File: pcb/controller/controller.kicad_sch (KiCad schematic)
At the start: 27 parts, among them J1 Conn_01x02, J10 USB_C_Receptacle_USB2.0_16P, J2 Conn_01x02, J3 Conn_01x02, J4 Conn_01x02, J5 Conn_01x02, J6 Conn_01x02, J7 Conn_01x02, J8 RJ45, U2 AP2112K-3.3

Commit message: Final Version of new Controller Rev. 00 (Prototype)
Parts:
- removed C3, C4: C, Capacitor_SMD:C_0805_2012Metric_Pad1.18x1.45mm_HandSolder, symbol Device:C
- removed J1, J2, J3, J4, J5, J6, J7: Conn_01x02, Connector_JST:JST_XH_B2B-XH-AM_1x02_P2.50mm_Vertical, symbol Connector_Generic:Conn_01x02
- removed J10: USB_C_Receptacle_USB2.0_16P, Connector_USB:USB_C_Receptacle_GCT_USB4105-xx-A_16P_TopMnt_Horizontal, symbol Connector:USB_C_Receptacle_USB2.0_16P
- removed J8: RJ45, RJ45:RJ45_Amphenol_54602-x08_Horizontal, symbol Connector:RJ45
- removed JP1: SolderJumper_2_Bridged, Jumper:SolderJumper-2_P1.3mm_Bridged_RoundedPad1.0x1.5mm, symbol Jumper:SolderJumper_2_Bridged
- removed JP2: SolderJumper_2_Open, Jumper:SolderJumper-2_P1.3mm_Open_RoundedPad1.0x1.5mm, symbol Jumper:SolderJumper_2_Open
- removed U1: ~, Heltec_WiFi_LoRa_V3:Heltec_WiFi_LoRa_V3, symbol Heltec_WiFi_Lora_V3:Heltec_WiFi_LoRa_V3
- removed U2: AP2112K-3.3, Package_TO_SOT_SMD:SOT-23-5, symbol Regulator_Linear:AP2112K-3.3
- added D1, D2: LED, LED_SMD:LED_0603_1608Metric, symbol Device:LED
- added D3: SMAJ24A, Diode_SMD:D_SMA, symbol Diode:SMAJ24A
- added J1, J4: Term 3.5mm, Connector_Phoenix_MC:PhoenixContact_MC_1,5_2-G-3.5_1x02_P3.50mm_Horizontal, symbol Connector:Screw_Terminal_01x02
- added J2, J3: RJ45, Connector_RJ:RJ45_Amphenol_RJHSE5380, symbol Connector:RJ45
- added P1: USB_C_Plug_USB2.0, Connector_USB:USB_C_Receptacle_G-Switch_GT-USB-7010ASV, symbol Connector:USB_C_Plug_USB2.0
- added Q1: 20N06, Package_SON:VSON-8_3.3x3.3mm_P0.65mm_NexFET, symbol Ravenspark:60N03D
- added R7: 1k, Resistor_SMD:R_0402_1005Metric, symbol Device:R
- added SW1, SW2: SW_4x3mm, RVNSPRK_Switch:SW_Push_4x3mm, symbol Switch:SW_Push
- added U1: ESP32-S3-MINI-1, Espressif:ESP32-S3-MINI-1U, symbol Espressif:ESP32-S3-MINI-1
- C1, C2: value C -> 100n; footprint Capacitor_SMD:C_0805_2012Metric_Pad1.18x1.45mm_HandSolder -> Capacitor_SMD:C_0402_1005Metric
- H1, H2, H3, H4: value MountingHole -> M3; footprint MountingHole:MountingHole_3mm -> MountingHole:MountingHole_3.2mm_M3
- R1, R2, R4: value 10k -> 1k; footprint Resistor_SMD:R_0805_2012Metric_Pad1.20x1.40mm_HandSolder -> Resistor_SMD:R_0402_1005Metric
- R3: value 10k -> 1k; footprint Resistor_SMD:R_0805_2012Metric_Pad1.20x1.40mm_HandSolder -> Resistor_SMD:R_0402_1005Metric; now not fitted
- R5, R6: value 10k -> 4k3; footprint Resistor_SMD:R_0805_2012Metric_Pad1.20x1.40mm_HandSolder -> Resistor_SMD:R_0402_1005Metric
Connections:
- net 5V_IN is gone; now on net GND: C2.2
- net GPIO34 is gone; now on net +3.3V: R1.1
- net GPIO38 is gone; now on net +3.3V: R6.1
- net GPIO39 is gone; now on net +3.3V: R5.1
- net GPIO42 is gone; now on net +3.3V: R4.1
- net GND: now also C1.2, J1.2 (Pin_2), J2.6, J2.7, J2.8, J3.6, J3.7, J3.8, P1.A1 (GND), P1.A12 (GND), P1.B1 (GND), P1.B12 (GND), P1.S1 (SHIELD), Q1.1 (S), Q1.2 (S), Q1.3 (S), SW1.2, SW2.2, U1.1 (GND), U1.2 (GND), U1.42 (GND), U1.43 (GND), U1.46 (GND), U1.47 (GND), U1.48 (GND), U1.49 (GND), U1.50 (GND), U1.51 (GND), U1.52 (GND), U1.53 (GND), U1.54 (GND), U1.55 (GND), U1.56 (GND), U1.57 (GND), U1.58 (GND), U1.59 (GND), U1.60 (GND), U1.61 (GND), U1.62 (GND), U1.63 (GND), U1.64 (GND), U1.65 (GND); no longer C1.1, C2.1
- removed net 3V3: R1.2, R2.2, R3.2, R4.2, R5.2, R6.2
- net GPIO20 renamed Power Supply/VUSB
- net Power Supply/VUSB: now also P1.A4 (VBUS), P1.A9 (VBUS), P1.B4 (VBUS), P1.B9 (VBUS)
- net GPIO26 renamed +3.3V
- net +3.3V: now also R7.1, U1.3 (3V3)
- new net: D1.2 (A), R1.2
- new net: D3.2 (A2), J4.2 (Pin_2), Q1.5 (D)
- new net: C1.1, R4.2, SW1.1, U1.45 (EN)
- new net: D2.2 (A), R2.2
- new net +12V: D3.1 (A1), J4.1 (Pin_1)
- new net BOOT: C2.1, R7.2, SW2.1, U1.4 (GPIO0/BOOT)
- new net BTN_1: U1.7 (GPIO3/TOUCH3/ADC1_CH2)
- new net BTN_2: U1.8 (GPIO4/TOUCH4/ADC1_CH3)
- new net BTN_3: U1.9 (GPIO5/TOUCH5/ADC1_CH4)
- new net BTN_4: U1.10 (GPIO6/TOUCH6/ADC1_CH5)
- new net BTN_5: U1.11 (GPIO7/TOUCH7/ADC1_CH6)
- new net BTN_6: U1.14 (GPIO10/TOUCH10/ADC1_CH9/FSPICS0/FSPIIO4/SUBSPICS0)
- new net BTN_7: U1.44 (GPIO46)
- new net BTN_8: U1.41 (GPIO45)
- new net CHG_STAT: U1.22 (GPIO18/U1RXD/ADC2_CH7/CLK_OUT3)
- new net Communication/RS485.A: J2.1, J3.1
- new net Communication/RS485.B: J2.2, J3.2
- new net D_N: P1.A7 (D-), U1.23 (GPIO19/U1RTS/ADC2_CH8/CLK_OUT2/USB_D-)
- new net D_P: P1.A6 (D+), R3.2, U1.24 (GPIO20/U1CTS/ADC2_CH9/CLK_OUT1/USB_D+)
- new net HORN: Q1.4 (G), U1.19 (GPIO15/U0RTS/ADC2_CH4/XTAL_32K_P)
- new net I2C.SCL: R6.2, U1.13 (GPIO9/TOUCH9/ADC1_CH8/FSPIHD/SUBSPIHD)
- new net I2C.SDA: R5.2, U1.12 (GPIO8/TOUCH8/ADC1_CH7/SUBSPICS1)
- new net I_SENSE: U1.6 (GPIO2/TOUCH2/ADC1_CH1)
- new net LED.ERR: D2.1 (K), U1.20 (GPIO16/U0CTS/ADC2_CH5/XTAL_32K_N)
- new net LED.OK: D1.1 (K), U1.34 (GPIO38/FSPIWP/SUBSPIWP)
- new net LORA.BUSY: U1.31 (SPIIO6/GPIO35/FSPID/SUBSPID)
- new net LORA.IRQ: U1.32 (SPIIO7/GPIO36/FSPICLK/SUBSPICLK)
- new net LORA.NSS: U1.25 (GPIO21)
- new net LORA.RST: U1.30 (GPIO48/SPICLK_N/SUBSPICLK_N_DIFF)
- new net OLED_EN: U1.15 (GPIO11/TOUCH11/ADC2_CH0/FSPID/FSPIIO5/SUBSPID)
- new net PWR_SHDN: U1.21 (GPIO17/U1TXD/ADC2_CH6)
- new net SPI.CLK: U1.27 (GPIO47/SPICLK_P/SUBSPICLK_P_DIFF)
- new net SPI.MISO: U1.29 (SPIIO5/GPIO34/FSPICS0/SUBSPICS0)
- new net SPI.MOSI: U1.28 (SPIIO4/GPIO33/FSPIHD/SUBSPIHD)
- new net UART.RX: U1.17 (GPIO13/TOUCH13/ADC2_CH2/FSPIQ/FSPIIO7/SUBSPIQ)
- new net UART.TX: U1.16 (GPIO12/TOUCH12/ADC2_CH1/FSPICLK/FSPIIO6/SUBSPICLK)
- new net UART.TXEN: U1.18 (GPIO14/TOUCH14/ADC2_CH3/FSPIWP/FSPIDQS/SUBSPIWP)
- new net VBUS: J1.1 (Pin_1), J2.3, J2.4, J2.5, J3.3, J3.4, J3.5
- new net V_SENSE: U1.5 (GPIO1/TOUCH1/ADC1_CH0)
- no-connect marks 0 -> 10
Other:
- added sheet Communication (Communication.kicad_sch)
- added sheet Display & Buttons (Display.kicad_sch)
- added sheet Power Supply (Power_Supply.kicad_sch)
- note added: "BL Strap FLT"
- note added: "BL Strap PD"
- note added: "BL Strap PU"
- note added: "Reserved USB BL"
- note added: "USB BL In"
- note added: "USB BL Out"
- note removed: "Power"
- company: (none) -> Ravenspark
- title: (none) -> Open-Shot-Clock CONTROLLER

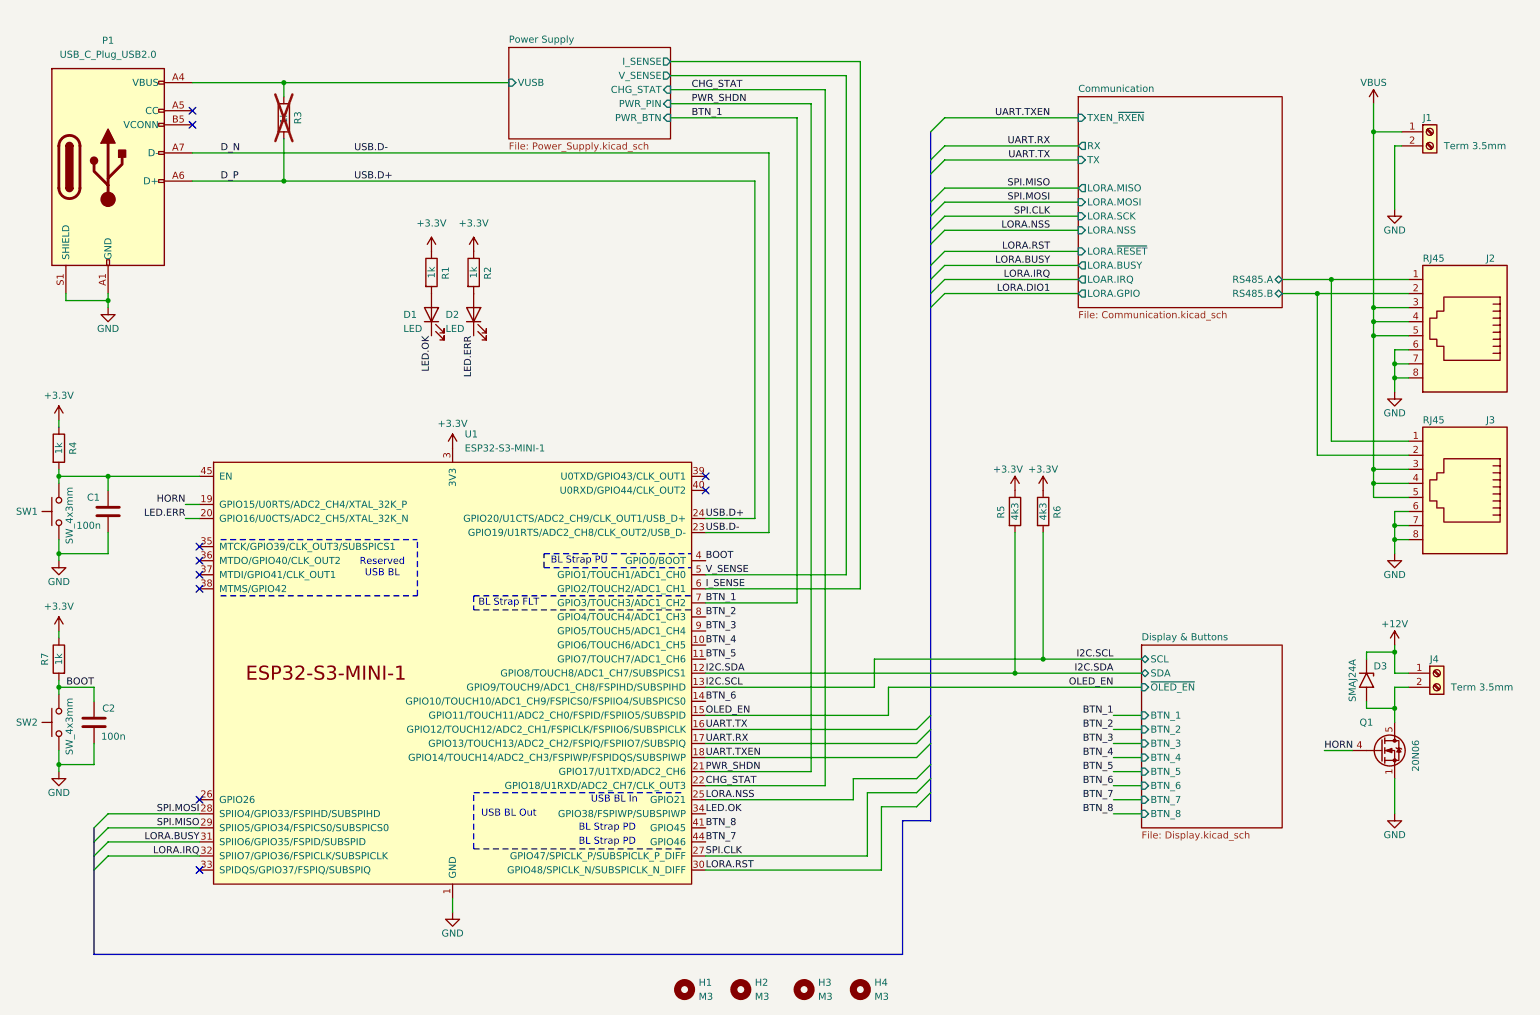
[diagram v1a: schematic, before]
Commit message: Revision 01 of Controller hardware
- fixed bugs from revision 00
- changed folder structure
- added ReleaseNotes_Controller.md to keep track of changes
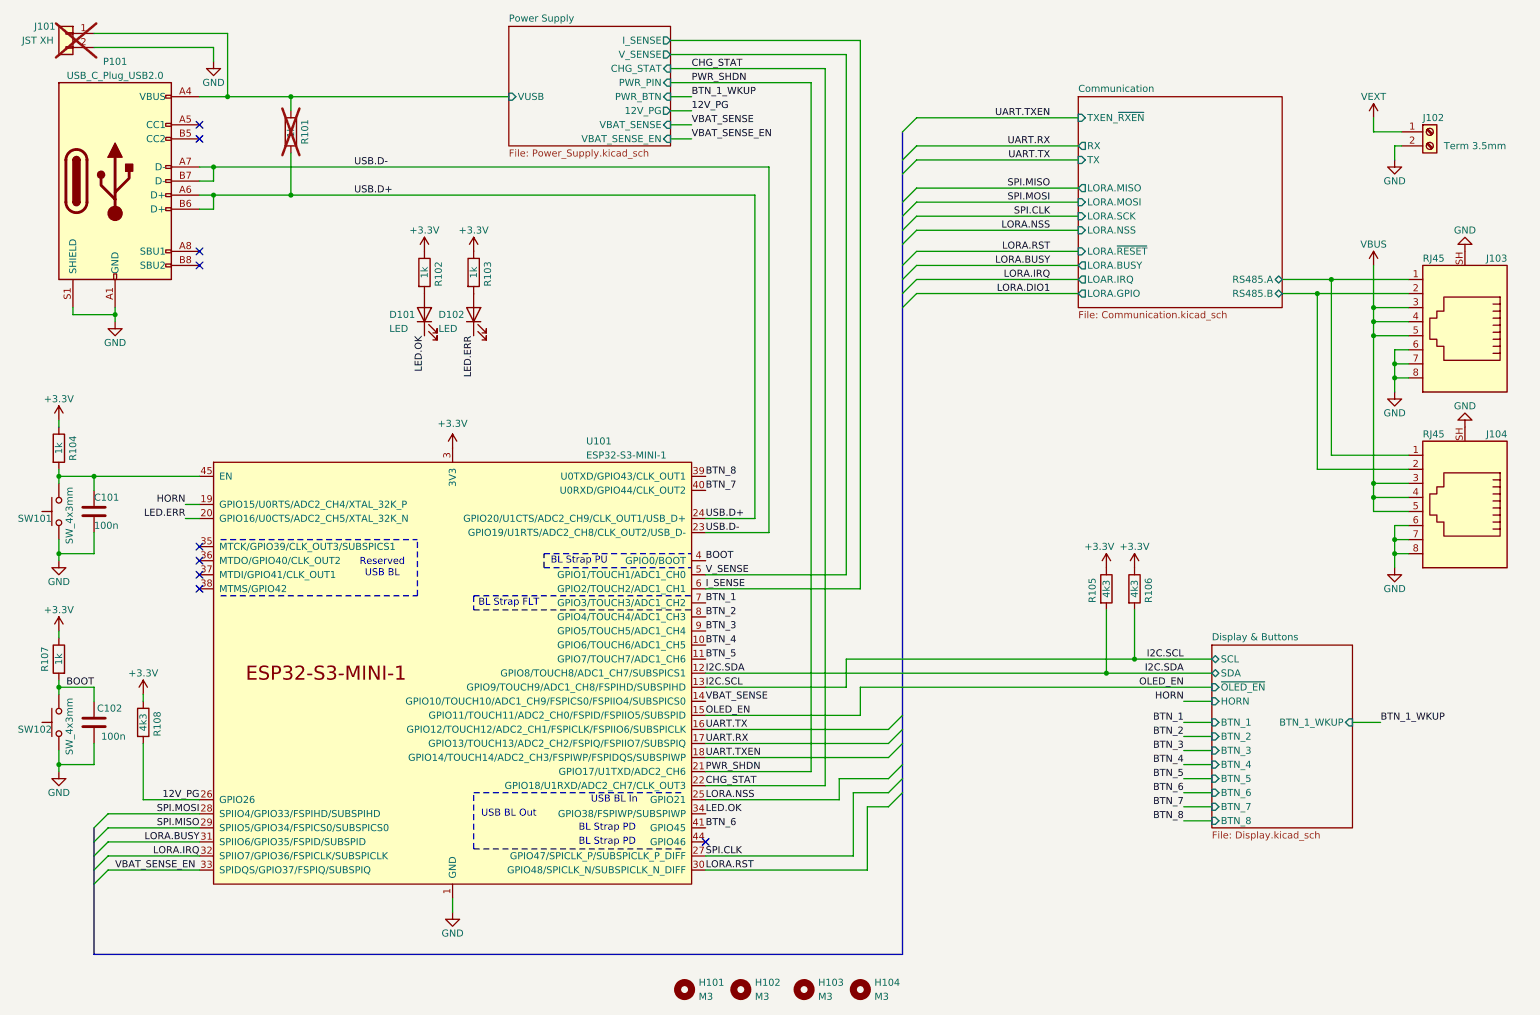
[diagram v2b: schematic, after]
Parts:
- removed D3: SMAJ24A, Diode_SMD:D_SMA, symbol Diode:SMAJ24A
- removed J4: Term 3.5mm, Connector_Phoenix_MC:PhoenixContact_MC_1,5_2-G-3.5_1x02_P3.50mm_Horizontal, symbol Connector:Screw_Terminal_01x02
- removed Q1: 20N06, Package_SON:VSON-8_3.3x3.3mm_P0.65mm_NexFET, symbol Ravenspark:60N03D
- added J101: JST XH, Connector_JST:JST_XH_B2B-XH-A_1x02_P2.50mm_Vertical, symbol Connector_Generic:Conn_01x02
- added R108: 4k3, Resistor_SMD:R_0402_1005Metric, symbol Device:R
- C101: renamed from C1; LCSC Part # (none) -> C307331
- C102: renamed from C2; LCSC Part # (none) -> C307331
- D101: renamed from D1; LCSC Part # (none) -> C2286
- D102: renamed from D2; LCSC Part # (none) -> C2286
- H101: renamed from H1; now in the parts list
- H102: renamed from H2; now in the parts list
- H103: renamed from H3; now in the parts list
- H104: renamed from H4; now in the parts list
- J102: renamed from J1; LCSC Part # (none) -> C409115
- J103: renamed from J2; symbol Connector:RJ45 -> Connector:RJ45_Shielded; LCSC Part # (none) -> C19078599
- J104: renamed from J3; symbol Connector:RJ45 -> Connector:RJ45_Shielded; LCSC Part # (none) -> C19078599
- P101: renamed from P1; symbol Connector:USB_C_Plug_USB2.0 -> Connector:USB_C_Receptacle_USB2.0_16P; LCSC Part # (none) -> C2927039
- SW101: renamed from SW1; LCSC Part # (none) -> C18078117
- SW102: renamed from SW2; LCSC Part # (none) -> C18078117
- U101: renamed from U1; LCSC Part # (none) -> C2980299
- renumbered R3 to R101, R1 to R102, R2 to R103, R4 to R104, R5 to R105, R6 to R106, R7 to R107
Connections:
- net +3.3V: now also R108.1
- net BTN_6: now also U101.41 (GPIO45); no longer U101.14 (GPIO10/TOUCH10/ADC1_CH9/FSPICS0/FSPIIO4/SUBSPICS0)
- net BTN_7: now also U101.40 (U0RXD/GPIO44/CLK_OUT2); no longer U101.44 (GPIO46)
- net BTN_8: now also U101.39 (U0TXD/GPIO43/CLK_OUT1); no longer U101.41 (GPIO45)
- net GND: now also J103.SH, J104.SH, J101.2 (Pin_2)
- net Power Supply/VUSB: now also J101.1 (Pin_1)
- net VBUS: no longer J102.1 (Pin_1)
- net 12V_PG: now reaches U101.26 (GPIO26)
- net 12V_PG: now also R108.2
- net VBAT_SENSE_EN: now reaches U101.33 (SPIDQS/GPIO37/FSPIQ/SUBSPIQ)
- net D_N renamed USB.D-
- net USB.D-: now also P101.B7 (D-)
- net D_P renamed USB.D+
- net USB.D+: now also P101.B6 (D+)
- new net VBAT_SENSE: U101.14 (GPIO10/TOUCH10/ADC1_CH9/FSPICS0/FSPIIO4/SUBSPICS0)
- new net VEXT: J102.1 (Pin_1)
- no-connect marks 10 -> 9
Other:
- sheet Display & Buttons ports: added BTN_1_WKUP, HORN; removed none
- sheet Power Supply ports: added 12V_PG, VBAT_SENSE, VBAT_SENSE_EN; removed none
- title: Open-Shot-Clock CONTROLLER -> Open Shot Clock - Controller
- moved on the sheet: C101, D101, R101, R102, R105, R106

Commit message: Final adjustments and BOM optimization
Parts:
- R108: value 4k3 -> 10k
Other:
- moved on the sheet: C102, D101, D102, R102, R103, R107, SW102

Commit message: Updated ReleaseNotes_Controller.md with know issues of R01
Changed SMD button JLC order number to version without mounting holes
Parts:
- SW101, SW102: LCSC Part # C18078117 -> C18077679
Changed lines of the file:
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@@
 			)
 		)
-		(property "LCSC Part #" "C18078117"
+		(property "LCSC Part #" "C18077679"
 			(at 20.32 105.41 0)
 			(effects
@@
 			)
 		)
-		(property "LCSC Part #" "C18078117"
+		(property "LCSC Part #" "C18077679"
 			(at 60.96 74.93 0)
 			(effects
